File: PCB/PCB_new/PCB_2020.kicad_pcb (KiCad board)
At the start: 2 copper layers, 102.2 x 94.5 mm, 32 parts, among them IC1 LM358N, Q1 220mA/50V/3.5Ω, Q2 100V/17A, Q3 100V/17A, Q4 100V/17A, Q5 100V/17A, Q6 100V/17A, Q7 220mA/50V/3.5Ω, Q8 220mA/50V/3.5Ω, U1 TI_CONN

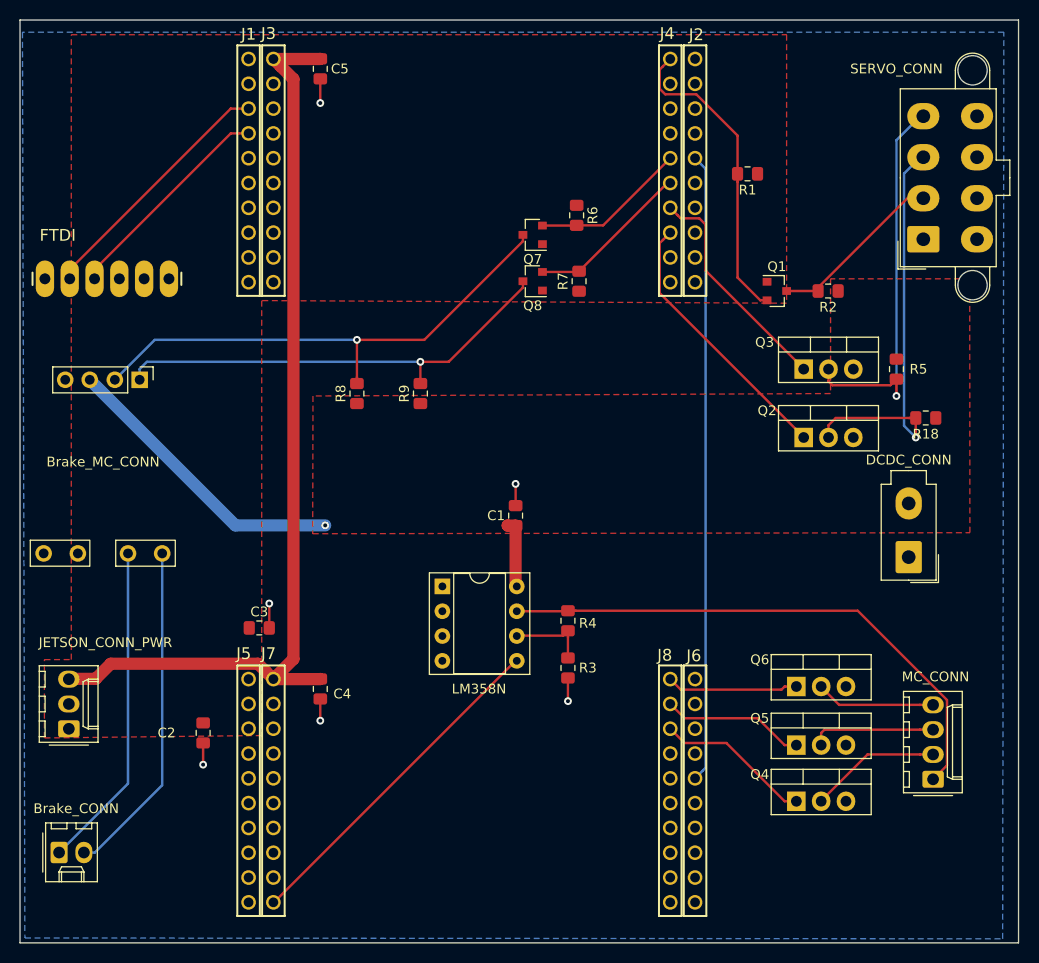
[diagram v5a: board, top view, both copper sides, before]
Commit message: added mounting holes
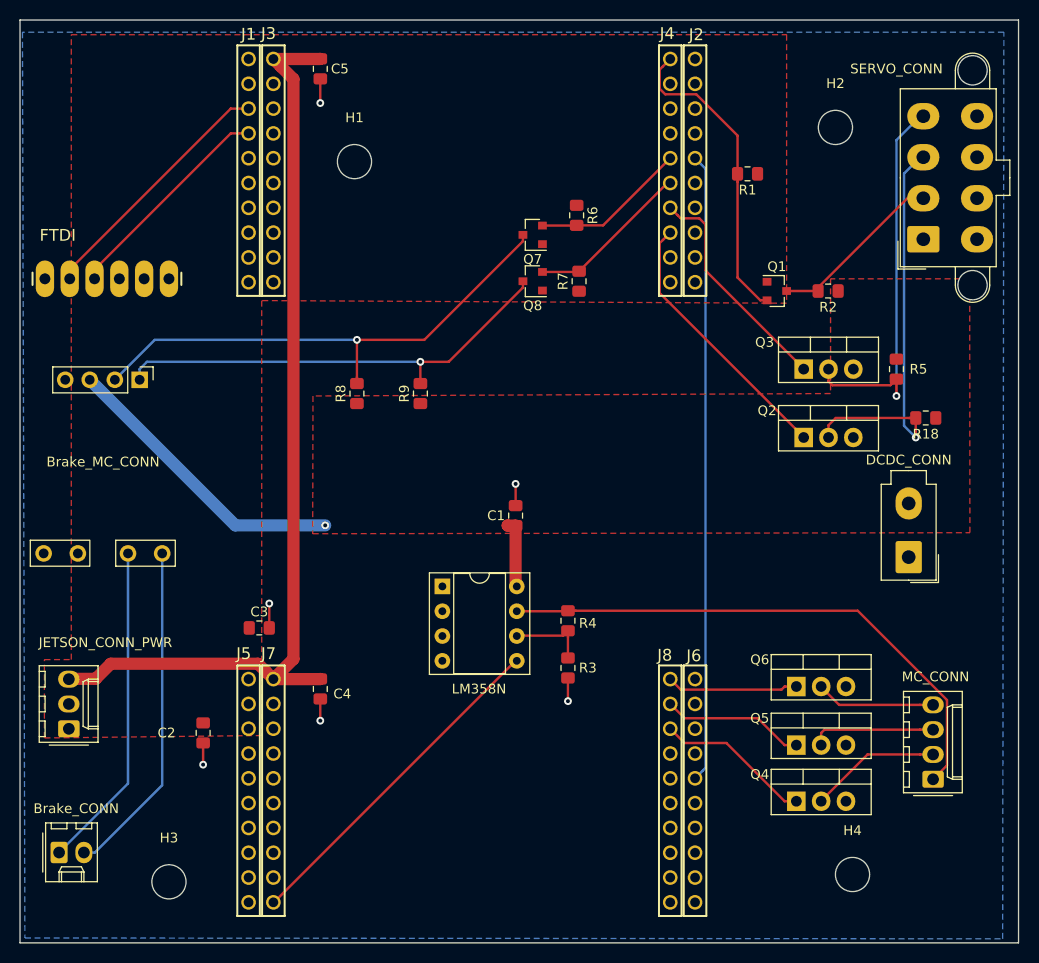
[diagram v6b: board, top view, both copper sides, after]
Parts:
- added H1: MountingHole, MountingHole:MountingHole_3.5mm, F.Cu at (130.0, 61.2)
- added H2: MountingHole, MountingHole:MountingHole_3.5mm, F.Cu at (179.2, 57.8)
- added H3: MountingHole, MountingHole:MountingHole_3.5mm, F.Cu at (111.0, 135.0)
- added H4: MountingHole, MountingHole:MountingHole_3.5mm, F.Cu at (181.0, 134.2)
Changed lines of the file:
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@@
     (tracks 158)
     (zones 0)
-    (modules 32)
+    (modules 36)
     (nets 29)
   )
@@
     (add_net "/LAUNCHXL-F28379D Breakout/REV_MC")
     (add_net "/LAUNCHXL-F28379D Breakout/THROTTLE_MC")
+    (add_net "/LAUNCHXL-F28379D Headers/ADCA0")
+    (add_net "/LAUNCHXL-F28379D Headers/ADCIN1")
+    (add_net "/LAUNCHXL-F28379D Headers/ADCIN15")
+    (add_net "/LAUNCHXL-F28379D Headers/ADCINA2")
+    (add_net "/LAUNCHXL-F28379D Headers/ADCINA3")
+    (add_net "/LAUNCHXL-F28379D Headers/ADCINA4")
+    (add_net "/LAUNCHXL-F28379D Headers/ADCINA5")
+    (add_net "/LAUNCHXL-F28379D Headers/ADCINB2")
+    (add_net "/LAUNCHXL-F28379D Headers/ADCINB3")
+    (add_net "/LAUNCHXL-F28379D Headers/ADCINB4")
+    (add_net "/LAUNCHXL-F28379D Headers/ADCINB5")
+    (add_net "/LAUNCHXL-F28379D Headers/ADCINC2")
+    (add_net "/LAUNCHXL-F28379D Headers/ADCINC3")
+    (add_net "/LAUNCHXL-F28379D Headers/ADCINC4")
+    (add_net "/LAUNCHXL-F28379D Headers/ADCINC5")
+    (add_net "/LAUNCHXL-F28379D Headers/GPIO1-PWMOUT1B")
+    (add_net "/LAUNCHXL-F28379D Headers/GPIO104-I2CSDAA-J1")
+    (add_net "/LAUNCHXL-F28379D Headers/GPIO105-I2SSCLA-J1")
+    (add_net "/LAUNCHXL-F28379D Headers/GPIO111")
+    (add_net "/LAUNCHXL-F28379D Headers/GPIO122-SD1D1")
+    (add_net "/LAUNCHXL-F28379D Headers/GPIO123-SD1CLK1")
+    (add_net "/LAUNCHXL-F28379D Headers/GPIO124-SD1D2")
+    (add_net "/LAUNCHXL-F28379D Headers/GPIO125-SD1CLK2")
+    (add_net "/LAUNCHXL-F28379D Headers/GPIO130-SD2D1")
+    (add_net "/LAUNCHXL-F28379D Headers/GPIO131-SD2CLK1")
+    (add_net "/LAUNCHXL-F28379D Headers/GPIO139-SCICRX(->MCU)")
+    (add_net "/LAUNCHXL-F28379D Headers/GPIO15-OPXBAR4")
+    (add_net "/LAUNCHXL-F28379D Headers/GPIO2-PWMOUT2A")
+    (add_net "/LAUNCHXL-F28379D Headers/GPIO22")
+    (add_net "/LAUNCHXL-F28379D Headers/GPIO25-OPXBAR2")
+    (add_net "/LAUNCHXL-F28379D Headers/GPIO26-SD2D2")
+    (add_net "/LAUNCHXL-F28379D Headers/GPIO27-SD2CLK2")
+    (add_net "/LAUNCHXL-F28379D Headers/GPIO29-OPXBAR6")
+    (add_net "/LAUNCHXL-F28379D Headers/GPIO3-PWMOUT2B")
+    (add_net "/LAUNCHXL-F28379D Headers/GPIO32")
+    (add_net "/LAUNCHXL-F28379D Headers/GPIO52-J5")
+    (add_net "/LAUNCHXL-F28379D Headers/GPIO56-SCICTX(<-MCU)")
+    (add_net "/LAUNCHXL-F28379D Headers/GPIO58-SPIAMOSI")
+    (add_net "/LAUNCHXL-F28379D Headers/GPIO59-SPIAMISO")
+    (add_net "/LAUNCHXL-F28379D Headers/GPIO60-SPICLKA")
+    (add_net "/LAUNCHXL-F28379D Headers/GPIO61-SPIACS")
+    (add_net "/LAUNCHXL-F28379D Headers/GPIO63-SPIBMOSI")
+    (add_net "/LAUNCHXL-F28379D Headers/GPIO64-SPIBMISO")
+    (add_net "/LAUNCHXL-F28379D Headers/GPIO65-SPIBCLK")
+    (add_net "/LAUNCHXL-F28379D Headers/GPIO66-SPIBCS")
+    (add_net "/LAUNCHXL-F28379D Headers/GPIO67")
+    (add_net "/LAUNCHXL-F28379D Headers/GPIO94")
+    (add_net "/LAUNCHXL-F28379D Headers/PWM-BASED-DAC1")
+    (add_net "/LAUNCHXL-F28379D Headers/PWM-BASED-DAC2")
+    (add_net "/LAUNCHXL-F28379D Headers/PWM-BASED-DAC3")
+    (add_net "/LAUNCHXL-F28379D Headers/PWM-BASED-DAC4")
     (add_net "/LAUNCHXL-F28379D Headers/RESET")
     (add_net Brake_PWM_1)
@@
     (add_net GND)
     (add_net INPUT_A+_CTL)
+    (add_net "Net-(CONN1-Pad1)")
+    (add_net "Net-(CONN1-Pad5)")
     (add_net "Net-(IC1-Pad6)")
+    (add_net "Net-(U1-Pad42)")
+    (add_net "Net-(U1-Pad45)")
+    (add_net "Net-(U1-Pad49)")
+    (add_net "Net-(U1-Pad50)")
+    (add_net "Net-(U1-Pad74)")
+    (add_net "Net-(U1-Pad75)")
+    (add_net "Net-(U1-Pad76)")
+    (add_net "Net-(U1-Pad77)")
     (add_net REV_CTL)
     (add_net SCIB_RX)
@@
     (add_net +5V)
   )
+  (module MountingHole:MountingHole_3.5mm (layer Top)
+    (at 181 134.25)
+    (descr "Mounting Hole 3.5mm, no annular")
+    (tags "mounting hole 3.5mm no annular")
+    (attr virtual)
+    (fp_text reference H4 (at 0 -4.5) (layer F.SilkS)
+      (effects (font (size 1 1) (thickness 0.15)))
+    )
+    (fp_text value MountingHole (at 0 4.5) (layer F.Fab)
+      (effects (font (size 1 1) (thickness 0.15)))
+    )
+    (fp_circle (center 0 0) (end 3.75 0) (layer F.CrtYd) (width 0.05))
+    (fp_circle (center 0 0) (end 3.5 0) (layer Cmts.User) (width 0.15))
+    (fp_text user %R (at 0.3 0) (layer F.Fab)
+      (effects (font (size 1 1) (thickness 0.15)))
+    )
+    (pad 1 np_thru_hole circle (at 0 0) (size 3.5 3.5) (drill 3.5) (layers *.Cu *.Mask))
+  )
+  (module MountingHole:MountingHole_3.5mm (layer Top)
+    (at 111 135)
+    (descr "Mounting Hole 3.5mm, no annular")
+    (tags "mounting hole 3.5mm no annular")
+    (attr virtual)
+    (fp_text reference H3 (at 0 -4.5) (layer F.SilkS)
+      (effects (font (size 1 1) (thickness 0.15)))
+    )
+    (fp_text value MountingHole (at 0 4.5) (layer F.Fab)
+      (effects (font (size 1 1) (thickness 0.15)))
+    )
+    (fp_circle (center 0 0) (end 3.75 0) (layer F.CrtYd) (width 0.05))
+    (fp_circle (center 0 0) (end 3.5 0) (layer Cmts.User) (width 0.15))
+    (fp_text user %R (at 0.3 0) (layer F.Fab)
+      (effects (font (size 1 1) (thickness 0.15)))
+    )
+    (pad 1 np_thru_hole circle (at 0 0) (size 3.5 3.5) (drill 3.5) (layers *.Cu *.Mask))
+  )
+  (module MountingHole:MountingHole_3.5mm (layer Top)
+    (at 179.25 57.75)
+    (descr "Mounting Hole 3.5mm, no annular")
+    (tags "mounting hole 3.5mm no annular")
+    (attr virtual)
+    (fp_text reference H2 (at 0 -4.5) (layer F.SilkS)
+      (effects (font (size 1 1) (thickness 0.15)))
+    )
+    (fp_text value MountingHole (at 0 4.5) (layer F.Fab)
+      (effects (font (size 1 1) (thickness 0.15)))
+    )
+    (fp_circle (center 0 0) (end 3.75 0) (layer F.CrtYd) (width 0.05))
+    (fp_circle (center 0 0) (end 3.5 0) (layer Cmts.User) (width 0.15))
+    (fp_text user %R (at 0.3 0) (layer F.Fab)
+      (effects (font (size 1 1) (thickness 0.15)))
+    )
+    (pad 1 np_thru_hole circle (at 0 0) (size 3.5 3.5) (drill 3.5) (layers *.Cu *.Mask))
+  )
+  (module MountingHole:MountingHole_3.5mm (layer Top)
+    (at 130 61.25)
+    (descr "Mounting Hole 3.5mm, no annular")
+    (tags "mounting hole 3.5mm no annular")
+    (attr virtual)
+    (fp_text reference H1 (at 0 -4.5) (layer F.SilkS)
+      (effects (font (size 1 1) (thickness 0.15)))
+    )
+    (fp_text value MountingHole (at 0 4.5) (layer F.Fab)
+      (effects (font (size 1 1) (thickness 0.15)))
+    )
+    (fp_circle (center 0 0) (end 3.75 0) (layer F.CrtYd) (width 0.05))
+    (fp_circle (center 0 0) (end 3.5 0) (layer Cmts.User) (width 0.15))
+    (fp_text user %R (at 0.3 0) (layer F.Fab)
+      (effects (font (size 1 1) (thickness 0.15)))
+    )
+    (pad 1 np_thru_hole circle (at 0 0) (size 3.5 3.5) (drill 3.5) (layers *.Cu *.Mask))
+  )
   (module Resistor_SMD:R_0805_2012Metric_Pad1.15x1.40mm_HandSolder (layer Top)

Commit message: removed unneeded level shifters
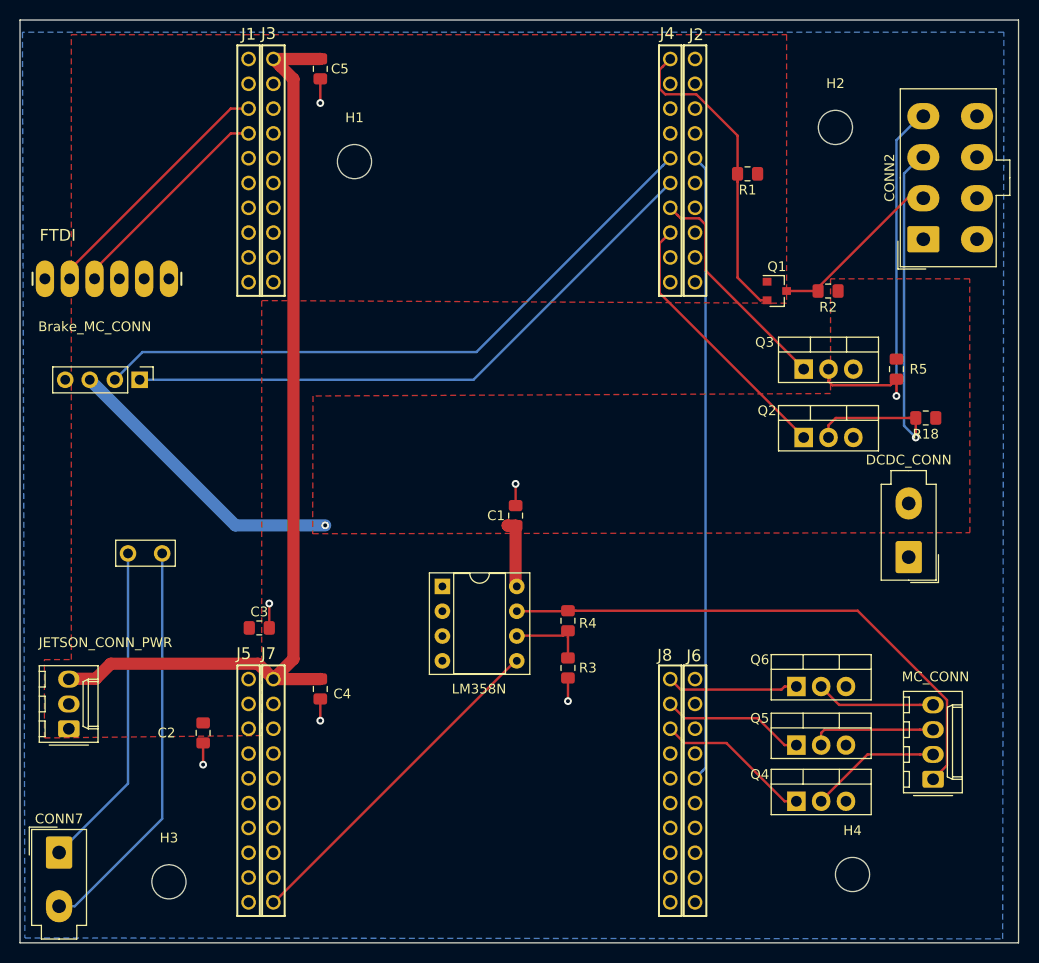
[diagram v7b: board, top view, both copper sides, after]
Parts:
- removed Q7, Q8: 220mA/50V/3.5Ω, Package_TO_SOT_SMD:SOT-23
- removed R6, R7, R8, R9: 10k, Resistor_SMD:R_0805_2012Metric_Pad1.15x1.40mm_HandSolder
- CONN2: footprint Connector_Molex:Molex_Mini-Fit_Jr_5566-08A2_2x04_P4.20mm_Vertical -> Connector_Molex:Molex_Mini-Fit_Jr_5566-08A_2x04_P4.20mm_Vertical
- CONN6: footprint Drivetrain_control:Brake_MC_Conn -> Drivetrain_control:Brake_MC_Conn_6pin
- CONN7: footprint Connector_Molex:Molex_KK-254_AE-6410-02A_1x02_P2.54mm_Vertical -> Connector_Molex:Molex_Mini-Fit_Jr_5566-02A_2x01_P4.20mm_Vertical
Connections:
- CONN6 pad 1: /LAUNCHXL-F28379D Breakout/Brake_Ctr_2 -> Brake_PWM_2
- CONN6 pad 2: /LAUNCHXL-F28379D Breakout/Brake_Ctr_1 -> Brake_PWM_1
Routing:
- net /LAUNCHXL-F28379D Breakout/Brake_Ctr_1: track 53.5 -> 0.00 mm, vias 1 -> 0
- net Brake_PWM_1: track 15.9 -> 66.3 mm
- net /LAUNCHXL-F28379D Breakout/Brake_Ctr_2: track 46.7 -> 0.00 mm, vias 1 -> 0
- net Brake_PWM_2: track 16.9 -> 62.7 mm
- net /LAUNCHXL-F28379D Breakout/Brake_Out_1: track 34.6 -> 41.4 mm

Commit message: changed mosfet type and package for level shifter circuit
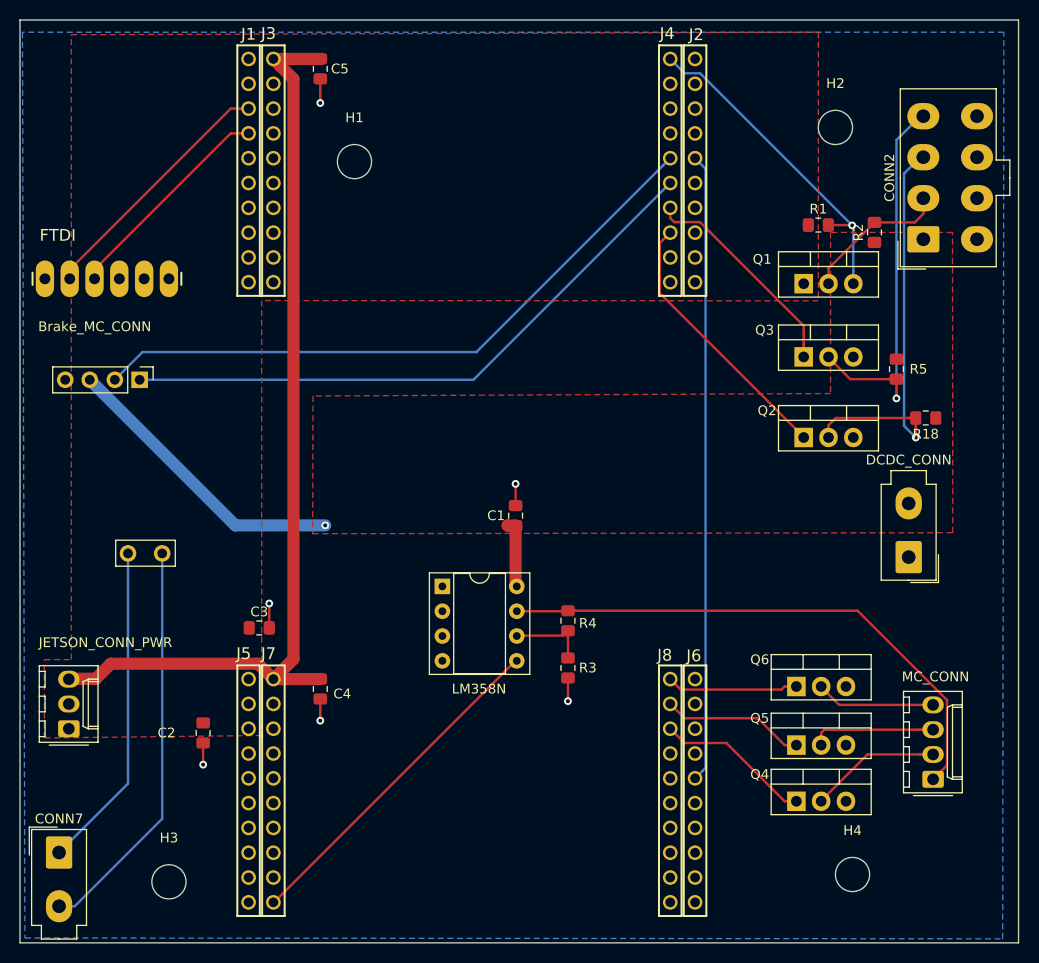
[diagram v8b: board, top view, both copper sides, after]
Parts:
- Q1: value 220mA/50V/3.5Ω -> 100V/17A; footprint Package_TO_SOT_SMD:SOT-23 -> Package_TO_SOT_THT:TO-220-3_Vertical
- moved R1 8.95 mm to (177.5, 67.8), turned to 0 degrees
- moved R2 7.65 mm to (183.2, 68.5), turned to 90 degrees
- moved Q1 2.85 mm to (176.0, 73.8)
- moved Q3 1.25 mm to (176.0, 81.2)
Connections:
- Q1 pad 2: TI_PWM -> /LAUNCHXL-F28379D Breakout/INPUT_B+
- Q1 pad 3: /LAUNCHXL-F28379D Breakout/INPUT_B+ -> TI_PWM
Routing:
- net /LAUNCHXL-F28379D Breakout/INPUT_B+: track 17.9 -> 15.2 mm
- net TI_PWM: track 32.0 -> 34.2 mm, vias 0 -> 1
- net EN+_CTL: track 23.3 -> 22.5 mm
- net /LAUNCHXL-F28379D Breakout/EN+: track 40.3 -> 40.1 mm, vias 1 -> 2
